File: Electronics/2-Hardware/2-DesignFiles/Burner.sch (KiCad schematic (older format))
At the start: 25 parts, among them P1 CONN_2, P2 CONN_2, P3 CONN_1, P5 CONN_2, P6 CONN_1, Q1 DMN2230U-7, U2 MSP430G2553-20, U3 ISL32612

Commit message: Updated reverse battery protection
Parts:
- removed Q?: MOS_P, ~, symbol MOS_P
- added C? (x6): C, symbol C
- added C?: 1uF, symbol C
- added D?: DIODE, symbol DIODE
- added L?: INDUCTOR_SMALL, symbol INDUCTOR_SMALL
- added Q?: DMN2230U-7, ~, symbol MOSFET_N
- added Q?: PMOS_POWER, symbol PMOS_POWER
- added R? (x5): R, symbol R
- added R? (x2): 121k, symbol R
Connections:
- wire segments 88 -> 177
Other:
- moved on the sheet: C1, P1, P?, R?, U2, U?

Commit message: Updated symbols on schematic
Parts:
- removed U? (x2): ADA4805-1, symbol ADA4805-1
- removed U?: LM3481, symbol LM3481
- added U?: LM3481, VSSOP-10, symbol LM3481
- added U? (x2): ADA4805-1, SOT-23-6, symbol ADA4805-1
- Q1: value DMN2230U-7 -> IRL6342; DigikeyPart DMN2230U-7DICT-ND -> IRL6342TRPBFCT-ND; Manufacturer Diodes Incorporated -> International Rectifier; ManufacturerNumber DMN2230U-7 -> IRL6342TRPBF
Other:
- note added: "Battery Input"
- moved on the sheet: C1, C2, P1, P2, P5, P?, Q?, R?, U2

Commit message: Added input circuitry, expansion port, power rails
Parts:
- removed C2: 0.1uF, ~, symbol C
- removed P5: CONN_2, ~, symbol CONN_2
- removed U3: ISL32612, symbol DIFF_RX
- added C? (x2): C, symbol C
- added D? (x2): 3V, symbol ZENER
- added P?: CONN_01X03, symbol CONN_01X03
- added P?: CONN_01X04, symbol CONN_01X04
- added Q?: PMOS, symbol PMOS_3-Term
- added R? (x2): 100, symbol R
- added R?: 240, symbol R
- added R?: 400, symbol R
- added U? (x2): LINEAR_REGULATOR, symbol LINEAR_REGULATOR
- C?: value C -> 10n
- C?: value 1uF -> 470n
- C? (x2): value C -> 390u
- C?: value C -> 47n
- C?: value C -> 2.2n
- C?: value C -> 1u
- L?: value INDUCTOR_SMALL -> 1.8u
- R?: value R -> 3m
- R?: value R -> 40.2k
- R?: value R -> 1k
- R?: value R -> 8.45k
- R?: value 121k -> 41.2k
- R?: value 121k -> 45.3k
- R?: value R -> 3.16k
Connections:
- net labels added: +5V, DATA_OUT, EXPANSION
- net labels removed: +BATT
- wire segments 177 -> 174
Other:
- note added: "Expansion Header"
- note added: "GND"
- note added: "Input Circuitry\n20mA = Logic 1\n10mA = Logic 0\n100 Ohm Impedance"
- note removed: "Differential Input Circuitry"
- note removed: "High"
- note removed: "Low"
- note removed: "Power"
- moved on the sheet: C1, C?, D?, L?, P1, P2, P?, Q?, R?, U2, U?

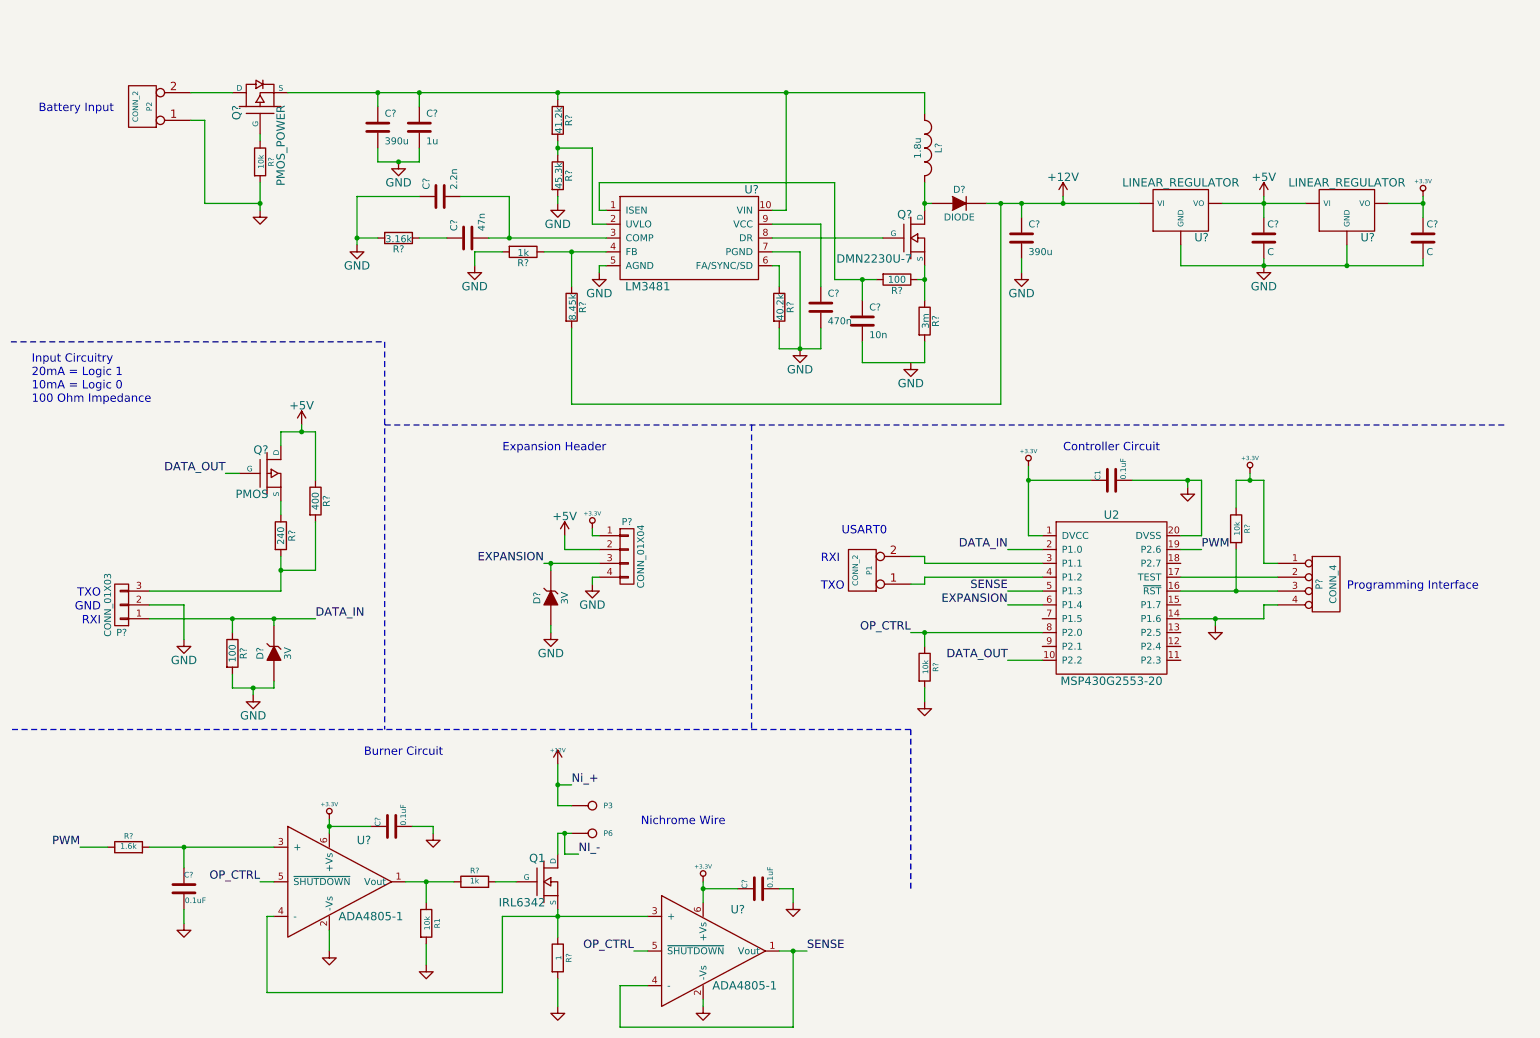
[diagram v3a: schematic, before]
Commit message: Worked on component footprint matching
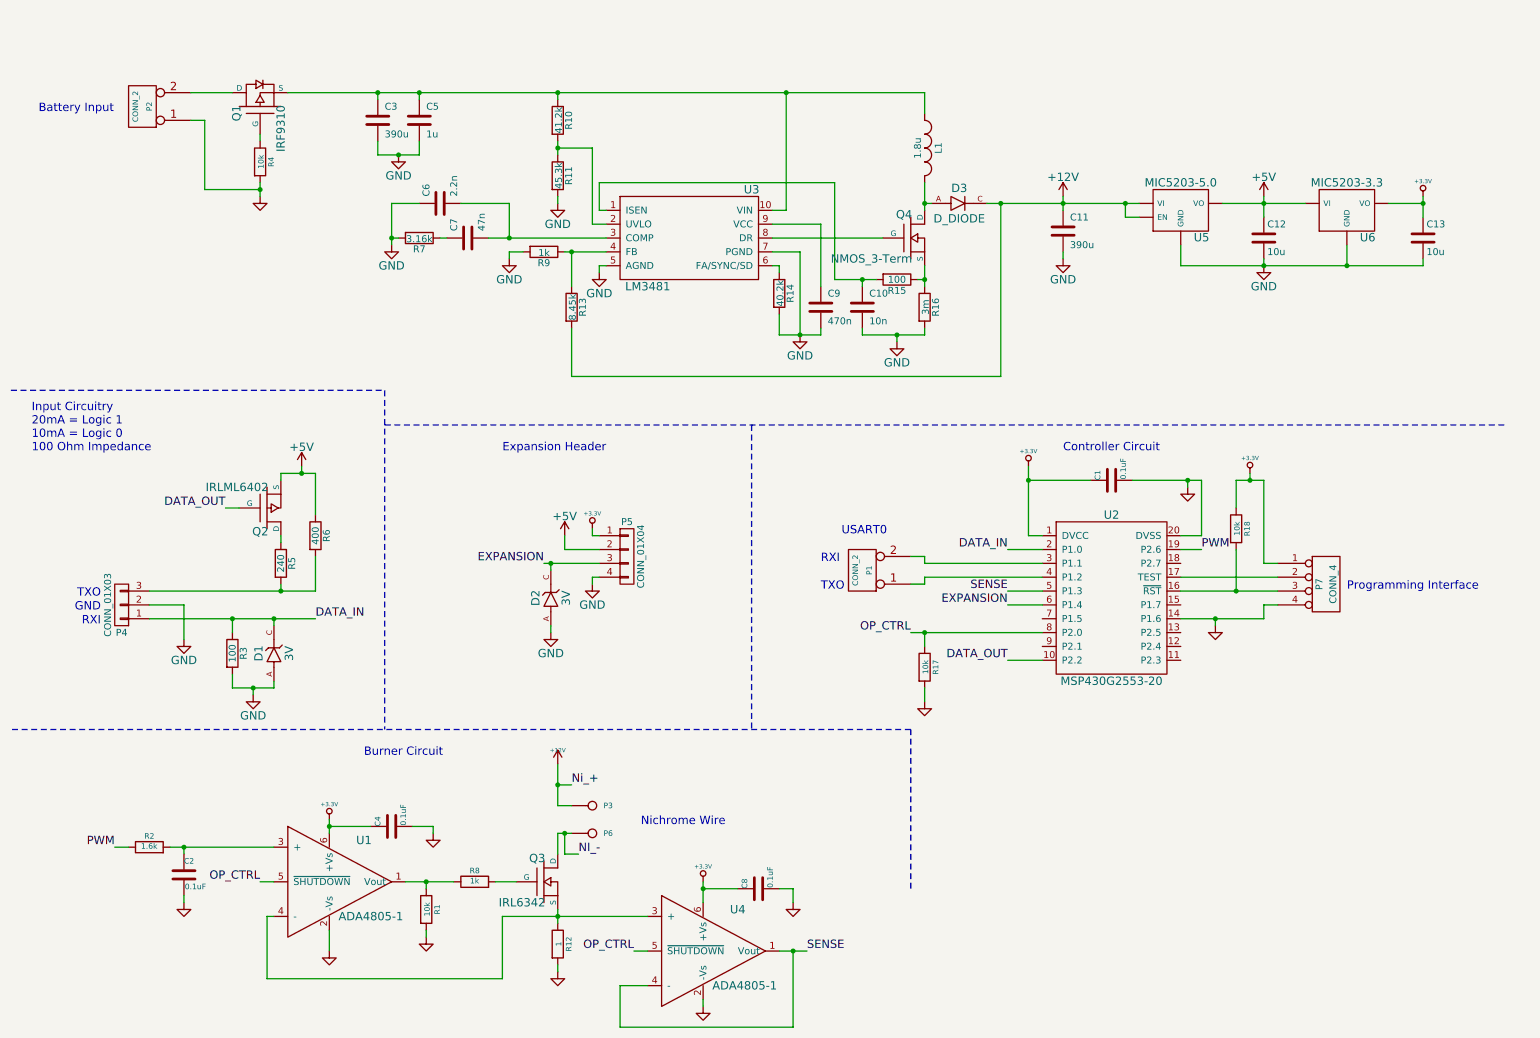
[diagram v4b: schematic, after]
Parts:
- removed D?: DIODE, symbol DIODE
- removed D? (x2): 3V, symbol ZENER
- removed Q1: IRL6342, ~, symbol MOSFET_N
- removed Q?: DMN2230U-7, ~, symbol MOSFET_N
- removed Q?: PMOS_POWER, symbol PMOS_POWER
- removed Q?: PMOS, symbol PMOS_3-Term
- removed U?: LINEAR_REGULATOR, symbol LINEAR_REGULATOR
- added D1, D2: 3V, SMD:DIODE_SOT-23-3, symbol D_ZENER
- added D3: D_DIODE, symbol D_DIODE
- added Q1: IRF9310, Transistors:TRANS_SO_4.0mm_1.27mm_8, symbol PMOS_POWER
- added Q2: IRLML6402, Transistors:TRANS_SOT-23-3, symbol PMOS_3-Term
- added Q3: IRL6342, Transistors:TRANS_SO_4.0mm_1.27mm_8, symbol NMOS_3-Term
- added Q4: NMOS_3-Term, symbol NMOS_3-Term
- added U5: MIC5203-5.0, SMD:SOT-23-5, symbol LINEAR_REGULATOR_EN
- C1: footprint ~ -> Capacitors_SMD:C_0805_HandSoldering
- C10, C5, C6, C7, C9: renamed from C?; footprint (none) -> Capacitors_SMD:C_0805_HandSoldering
- C12, C13: renamed from C?; value C -> 10u; footprint (none) -> Capacitors_SMD:C_0805_HandSoldering
- C2, C4, C8: renamed from C?; footprint ~ -> Capacitors_SMD:C_0805_HandSoldering
- P1, P2: footprint ~ -> Footprints:CONN_1x2
- P3, P6: footprint ~ -> Footprints:CONN_1x1
- P4, P5: renamed from P?; footprint (none) -> Footprints:CONN_1x2
- P7: renamed from P?; footprint ~ -> Footprints:CONN_1x4
- R1: footprint ~ -> Resistors_SMD:R_0805_HandSoldering
- R10, R11, R13, R14, R15, R3, R5, R6, R7, R9: renamed from R?; footprint (none) -> Resistors_SMD:R_0805_HandSoldering
- R12: renamed from R?; footprint ~ -> SMD:RES_D2PACK; DigikeyNumber (none) -> PWR163S-25-1R00J-ND; Manufacturer (none) -> Bournes; ManufacturerNumber (none) -> PWR163S-25-1R00J
- R16: renamed from R?; footprint (none) -> Footprints:SM2010; DigikeyNumber (none) -> RHM.003ASCT-ND; Manufacturer (none) -> Rohm Semiconductor; ManufacturerNumber (none) -> PMR50HZPFV3L00
- R17, R18, R2, R4, R8: renamed from R?; footprint ~ -> Resistors_SMD:R_0805_HandSoldering
- U1, U4: renamed from U?; footprint SOT-23-6 -> SMD:SOT-23-6
- U2: footprint ~ -> SMD:SOP_4.5mm_0.65mm_20
- U3: renamed from U?; footprint VSSOP-10 -> SMD:SOP_3.0mm_0.5mm_10
- U6: renamed from U?; value LINEAR_REGULATOR -> MIC5203-3.3; footprint (none) -> SMD:SOT-23-5; DigikeyNumber (none) -> 576-2728-1-ND; Manufacturer (none) -> Micrel; ManufacturerNumber (none) -> MIC5203-3.3YM5 TR
- gave numbers to parts that had none: 3
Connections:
- net +12V: now also D3.C, U5.1 (VI), U5.3 (EN)
- net +5V: now also Q2.S, U5.5 (VO)
- net DATA_IN: now also D1.C
- net DATA_OUT: now also Q2.G
- net EXPANSION: now also D2.C
- net GND: now also C10.2, R16.2, D1.A, D2.A, U5.2 (GND)
- net NI_-: now also Q3.D
- net at R8.2: now also Q3.G
- net at R12.1, U1.4 (-), U4.3 (+): now also Q3.S
- net at P2.2 (PM): now also Q1.D
- net at R4.1: now also Q1.G
- net at C3.1, C5.1, L1.1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: now also Q1.S
- net at L1.2: now also D3.A, Q4.D
- net at U3.8 (DR): now also Q4.G
- net at R15.1, R16.1: now also Q4.S
- net at R5.1: now also Q2.D
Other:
- moved on the sheet: C10, C11, C2, C3, C5, C6, R1, R12, R14, R16, R2, R5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

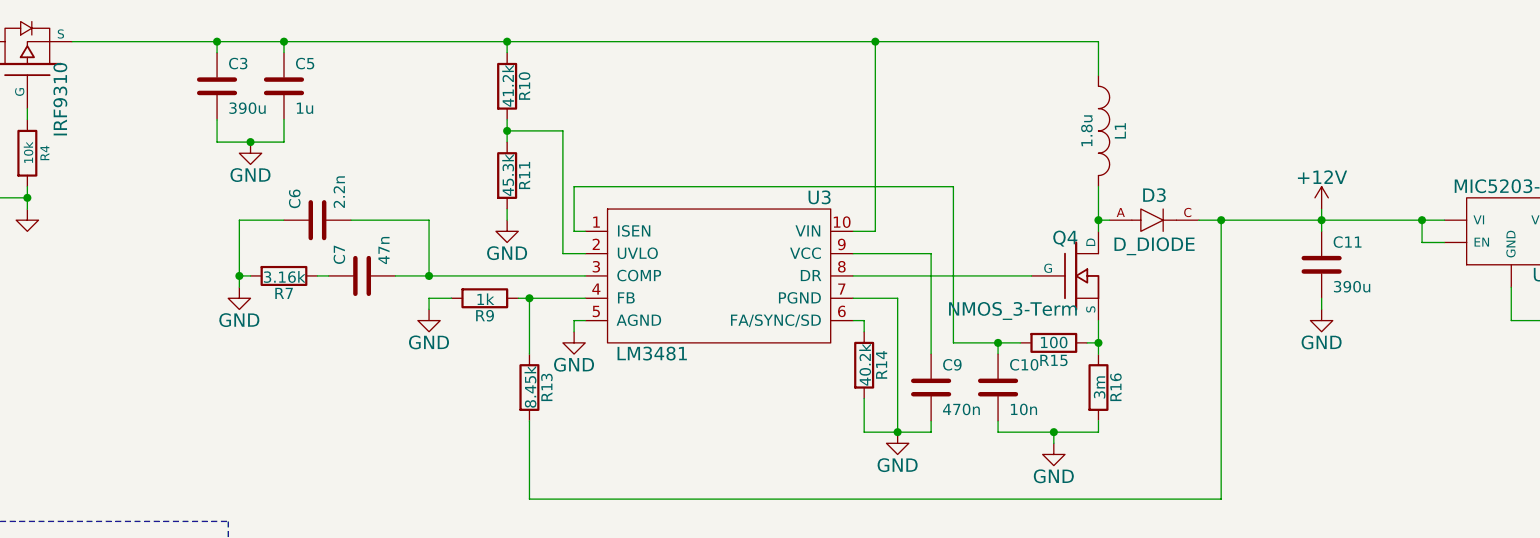
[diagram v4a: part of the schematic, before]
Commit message: Updated footprint association for capacitors
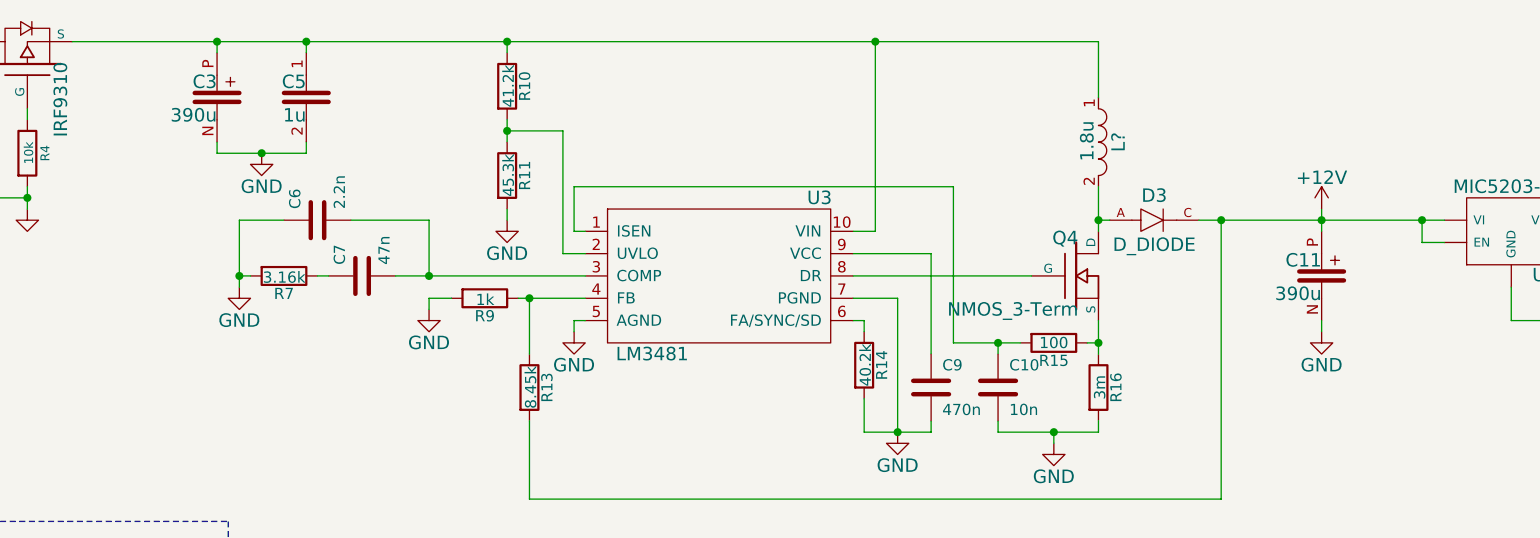
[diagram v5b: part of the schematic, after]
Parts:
- removed C11, C3: 390u, symbol C
- removed C5: 1u, Capacitors_SMD:C_0805_HandSoldering, symbol C
- removed L1: 1.8u, symbol INDUCTOR_SMALL
- added C11, C3: 390u, symbol CAP_POL
- added C5: 1u, symbol CAP
- added L?: 1.8u, symbol IND
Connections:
- net +12V: now also C11.P
- net GND: now also C11.N, C3.N, C5.2
- net at Q1.S, R10.1, U3.10 (VIN): now also C3.P, C5.1, L?.1
- net at D3.A, Q4.D: now also L?.2
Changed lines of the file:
@@
 LIBS:PowerComponents
 LIBS:Diodes
+LIBS:Passives
 LIBS:Burner-cache
 EELAYER 25 0
@@
 	2750 6100 3050 6100
 Connection ~ 2750 6100
-$Comp
-L INDUCTOR_SMALL L1
-U 1 1 54F6A58A
-P 7050 1200
-F 0 "L1" H 7050 1300 50  0000 C CNN
-F 1 "1.8u" H 7050 1150 50  0000 C CNN
-F 2 "" H 7050 1200 60  0001 C CNN
-F 3 "" H 7050 1200 60  0000 C CNN
-	1    7050 1200
-	0    1    1    0
-$EndComp
 Wire Wire Line
 	6750 1850 5950 1850
@@
 	7500 1600 8600 1600
 Wire Wire Line
-	7050 800  7050 950
+	7050 800  7050 1050
 Wire Wire Line
 	6050 800  6050 800
@@
 	4400 1550 4400 1600
 $Comp
-L C C11
-U 1 1 54F6C219
-P 8050 1800
-F 0 "C11" H 8100 1900 50  0000 L CNN
-F 1 "390u" H 8100 1700 50  0000 L CNN
-F 2 "" H 8088 1650 30  0001 C CNN
-F 3 "" H 8050 1800 60  0000 C CNN
-	1    8050 1800
-	1    0    0    -1
-$EndComp
-$Comp
 L GND #PWR022
 U 1 1 54F6C261
-P 8050 2000
-F 0 "#PWR022" H 8050 1750 60  0001 C CNN
-F 1 "GND" H 8050 1850 60  0000 C CNN
-F 2 "" H 8050 2000 60  0000 C CNN
-F 3 "" H 8050 2000 60  0000 C CNN
-	1    8050 2000
-	1    0    0    -1
-$EndComp
-Wire Wire Line
-	8050 1950 8050 2000
+P 8050 2100
+F 0 "#PWR022" H 8050 1850 60  0001 C CNN
+F 1 "GND" H 8050 1950 60  0000 C CNN
+F 2 "" H 8050 2100 60  0000 C CNN
+F 3 "" H 8050 2100 60  0000 C CNN
+	1    8050 2100
+	1    0    0    -1
+$EndComp
 Connection ~ 7600 1600
-$Comp
-L C C3
-U 1 1 54F6C41D
-P 3100 1000
-F 0 "C3" H 3150 1100 50  0000 L CNN
-F 1 "390u" H 3150 900 50  0000 L CNN
-F 2 "" H 3138 850 30  0001 C CNN
-F 3 "" H 3100 1000 60  0000 C CNN
-	1    3100 1000
-	1    0    0    -1
-$EndComp
 $Comp
 L GND #PWR023
 U 1 1 54F6C460
-P 3250 1250
-F 0 "#PWR023" H 3250 1000 60  0001 C CNN
-F 1 "GND" H 3250 1100 60  0000 C CNN
-F 2 "" H 3250 1250 60  0000 C CNN
-F 3 "" H 3250 1250 60  0000 C CNN
-	1    3250 1250
-	1    0    0    -1
-$EndComp
-Wire Wire Line
-	3100 1150 3100 1250
+P 3300 1300
+F 0 "#PWR023" H 3300 1050 60  0001 C CNN
+F 1 "GND" H 3300 1150 60  0000 C CNN
+F 2 "" H 3300 1300 60  0000 C CNN
+F 3 "" H 3300 1300 60  0000 C CNN
+	1    3300 1300
+	1    0    0    -1
+$EndComp
+Wire Wire Line
+	3100 1250 3100 1300
 $Comp
 L +12V #PWR024
@@
 	4050 1600 4050 1850
 Connection ~ 4050 1850
-$Comp
-L C C5
-U 1 1 54F6DF2C
-P 3400 1000
-F 0 "C5" H 3450 1100 50  0000 L CNN
-F 1 "1u" H 3450 900 50  0000 L CNN
-F 2 "Capacitors_SMD:C_0805_HandSoldering" H 3438 850 30  0001 C CNN
-F 3 "" H 3400 1000 60  0000 C CNN
-	1    3400 1000
-	1    0    0    -1
-$EndComp
-Wire Wire Line
-	3100 1250 3400 1250
-Wire Wire Line
-	3400 1250 3400 1150
-Connection ~ 3250 1250
+Wire Wire Line
+	3100 1300 3500 1300
+Connection ~ 3300 1300
 Text Notes 650  950  0    60   ~ 0
 Battery Input
@@
 Connection ~ 4400 800
 Wire Wire Line
-	3400 800  3400 850
-Connection ~ 3400 800
+	3500 800  3500 850
+Connection ~ 3500 800
 Text Label 7650 4100 2    60   ~ 0
 DATA_IN
@@
 	1    0    0    -1
 $EndComp
+Wire Wire Line
+	3500 1300 3500 1250
+$Comp
+L CAP_POL C3
+U 1 1 550929F3
+P 3100 1050
+F 0 "C3" H 3100 1120 60  0000 R CNN
+F 1 "390u" H 3100 970 60  0000 R CNN
+F 2 "" V 2840 950 60  0001 C CNN
+F 3 "" V 2940 1050 60  0001 C CNN
+	1    3100 1050
+	1    0    0    -1
+$EndComp
+$Comp
+L CAP C5
+U 1 1 55092BA7
+P 3500 1050
+F 0 "C5" H 3500 1120 60  0000 R CNN
+F 1 "1u" H 3500 970 60  0000 R CNN
+F 2 "" V 3240 950 60  0001 C CNN
+F 3 "" V 3340 1050 60  0001 C CNN
+	1    3500 1050
+	1    0    0    -1
+$EndComp
+$Comp
+L CAP_POL C11
+U 1 1 55093230
+P 8050 1850
+F 0 "C11" H 8050 1920 60  0000 R CNN
+F 1 "390u" H 8050 1770 60  0000 R CNN
+F 2 "" V 7790 1750 60  0001 C CNN
+F 3 "" V 7890 1850 60  0001 C CNN
+	1    8050 1850
+	1    0    0    -1
+$EndComp
+Wire Wire Line
+	8050 2100 8050 2050
+$Comp
+L IND L?
+U 1 1 55093E99
+P 7050 1250
+F 0 "L?" V 7140 1250 60  0000 C CNN
+F 1 "1.8u" V 7000 1255 60  0000 C CNN
+F 2 "" H 7050 1250 60  0000 C CNN
+F 3 "" H 7050 1250 60  0000 C CNN
+	1    7050 1250
+	1    0    0    -1
+$EndComp

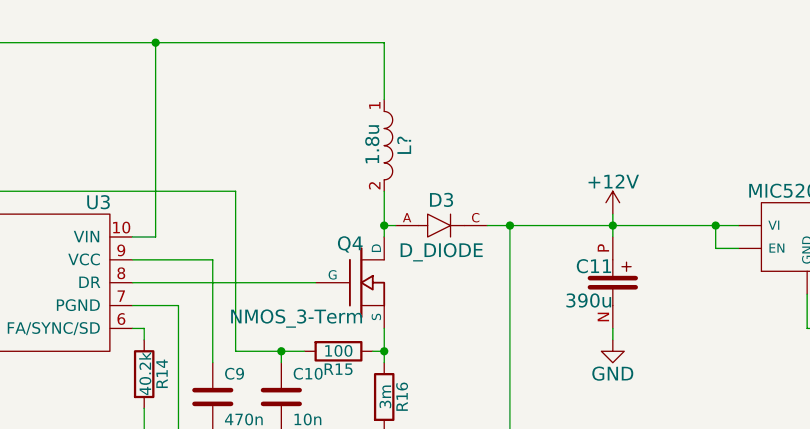
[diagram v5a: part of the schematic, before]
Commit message: Updated schematic and footprint association
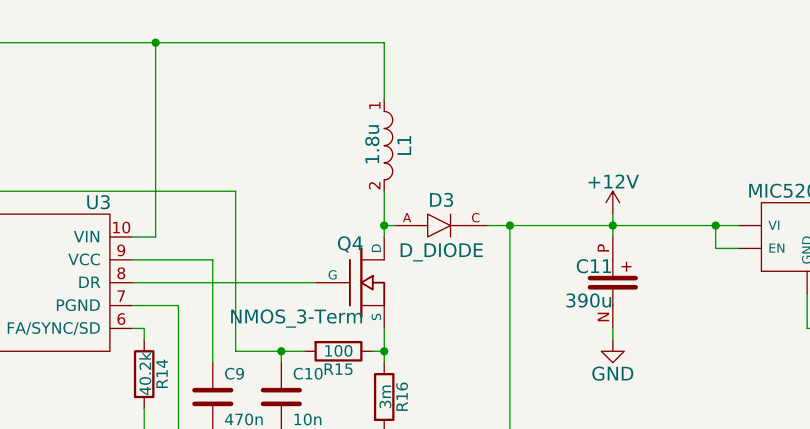
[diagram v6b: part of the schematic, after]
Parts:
- C11, C3: footprint (none) -> Capacitors:SMD_POL_E12_8.3mm
- C5: footprint (none) -> Capacitors_SMD:C_0805_HandSoldering
- gave numbers to parts that had none: 1
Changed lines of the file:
@@
 F 0 "C3" H 3100 1120 60  0000 R CNN
 F 1 "390u" H 3100 970 60  0000 R CNN
-F 2 "" V 2840 950 60  0001 C CNN
+F 2 "Capacitors:SMD_POL_E12_8.3mm" V 2840 950 60  0001 C CNN
 F 3 "" V 2940 1050 60  0001 C CNN
 	1    3100 1050
@@
 F 0 "C5" H 3500 1120 60  0000 R CNN
 F 1 "1u" H 3500 970 60  0000 R CNN
-F 2 "" V 3240 950 60  0001 C CNN
+F 2 "Capacitors_SMD:C_0805_HandSoldering" V 3240 950 60  0001 C CNN
 F 3 "" V 3340 1050 60  0001 C CNN
 	1    3500 1050
@@
 F 0 "C11" H 8050 1920 60  0000 R CNN
 F 1 "390u" H 8050 1770 60  0000 R CNN
-F 2 "" V 7790 1750 60  0001 C CNN
+F 2 "Capacitors:SMD_POL_E12_8.3mm" V 7790 1750 60  0001 C CNN
 F 3 "" V 7890 1850 60  0001 C CNN
 	1    8050 1850
@@
 	8050 2100 8050 2050
 $Comp
-L IND L?
+L IND L1
 U 1 1 55093E99
 P 7050 1250
-F 0 "L?" V 7140 1250 60  0000 C CNN
+F 0 "L1" V 7140 1250 60  0000 C CNN
 F 1 "1.8u" V 7000 1255 60  0000 C CNN
-F 2 "" H 7050 1250 60  0000 C CNN
+F 2 "" H 7050 1250 60  0001 C CNN
 F 3 "" H 7050 1250 60  0000 C CNN
 	1    7050 1250
